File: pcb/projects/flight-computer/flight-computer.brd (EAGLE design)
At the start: 101.6 x 60.6 mm, 92 parts, among them CN1 4U#20329, IC1 ADG609RU, IC2 ATSAMD21E, IC3 ADG609RU, P1 53048-0810, P2 53048-0810, U1 MCP73831/OT, U10 SN74LVC1G08DCKR, U12 MAX31856MUD+, U13 MAX31856MUD+, U2 LP2985IM5-1.8/NOPB, U3 COM-13909, U4 ADXL377, U5 ICM-20948, U6 PCA9306DCUR, U7 SN74LVC1T45DRLR, U8 SN74LVC1T45DRLR, U9 DMP3099L

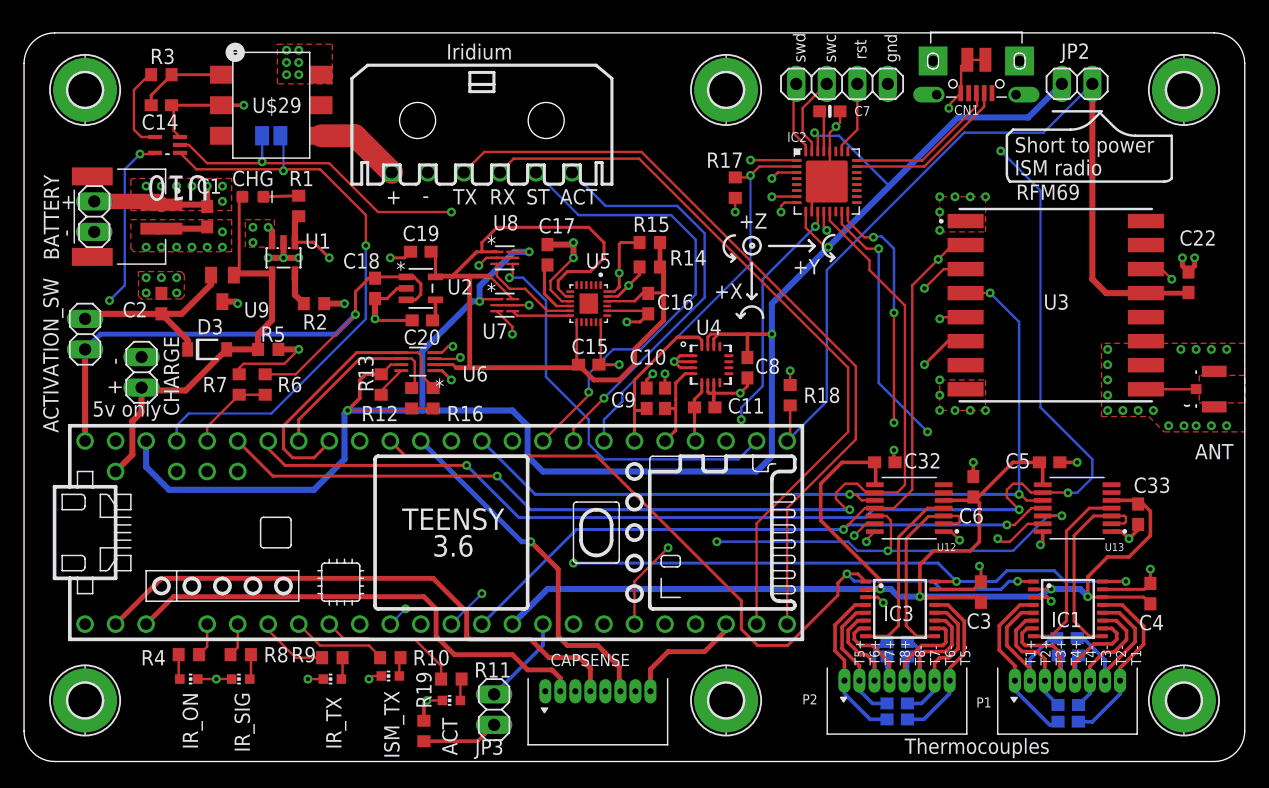
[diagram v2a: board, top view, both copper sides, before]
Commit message: add v1.1 pcb and documentation - added DSP310 barometric pressure sensor - add buzzer - add capacitive sense header - add more interface pins to the safety processor - add arduino pinouts for safety processor and refs on board silk - update flight computer hardware manual - add gerbers for v1.1 boards
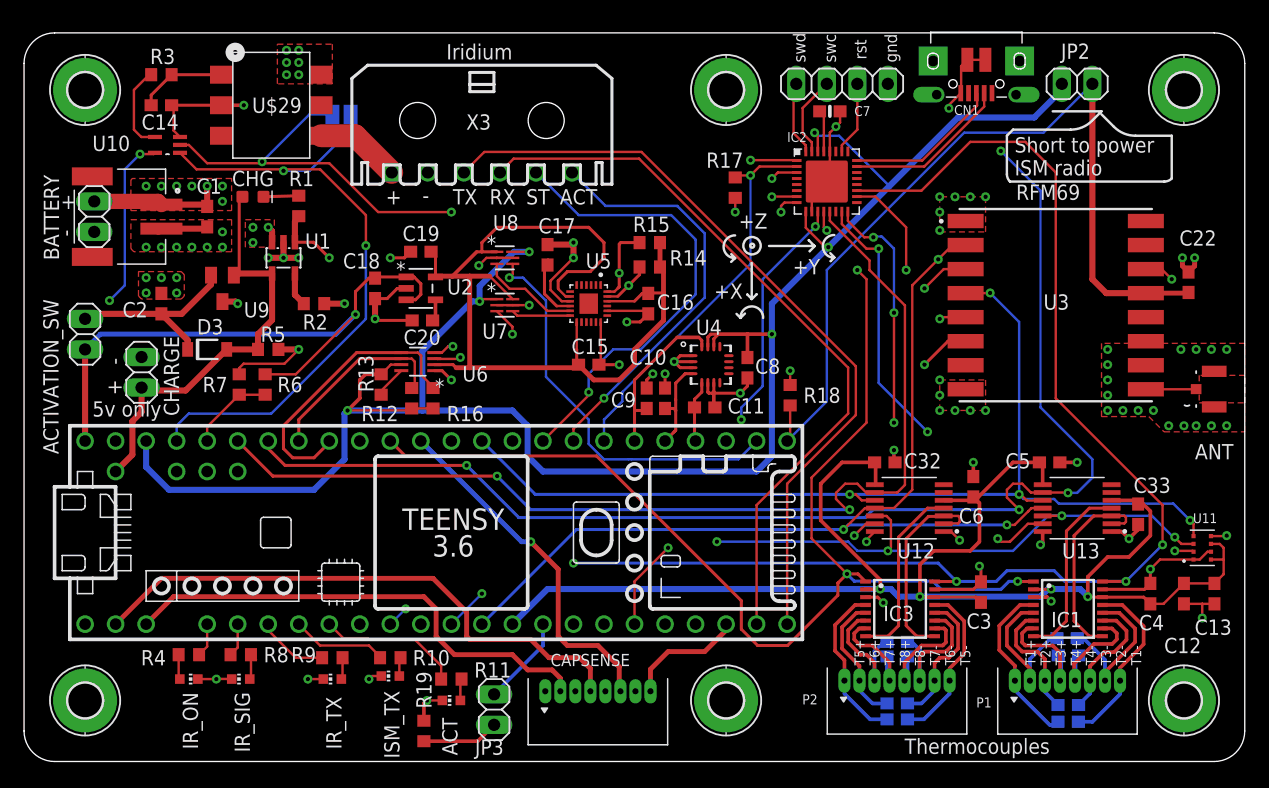
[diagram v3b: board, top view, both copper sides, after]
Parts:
- added C12, C13: 0.1uF, rcl:C0603
- added U11: DPS310XTSA1, DPS310XTSA1:XDCR_DPS310XTSA1
- moved SJ1 6.11 mm to (26.4, 53.8)
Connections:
- net SEC_CS renamed SEC_CTRL_2
- net SEC_EN renamed SEC_CTRL_1
- new net CS_DSP: U$1.8, U11.2
- net 3V3: now also C12.1, C13.1, U11.6, U11.8
- net GND: now also C12.2, C13.2, U11.1, U11.7
- net MISO: now also U11.5
- net MOSI: now also U11.3
- net MUX0: now also IC2.18
- net MUX1: now also IC2.19
- net SCLK: now also U11.4
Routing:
- net CS_DSP: track 0.00 -> 74.5 mm, vias 0 -> 1
- net MUX1: track 73.1 -> 131.4 mm, vias 3 -> 4
- net MUX0: track 67.6 -> 109.1 mm, vias 2 -> 4
- net MISO: track 92.5 -> 112.5 mm, vias 4 -> 5
- net SCLK: track 93.2 -> 109.7 mm, vias 4 -> 5
- net MOSI: track 112.1 -> 124.0 mm, vias 6 -> 7
- net 3V3: track 312.8 -> 324.7 mm
- net GND: track 133.2 -> 142.6 mm, vias 81 -> 82
- net SEC_ACT: track 57.8 -> 63.1 mm
- net PRI_ACT: track 50.1 -> 55.4 mm
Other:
- board text added: "0 CAPSENSE0 1 CAPSENSE1 3 LED1 (IR_ON) 4 LED2 (IR_SIG) 5 LED3 (IR_TX) 6 LED4 (ISM_TX) 7 LED5 (ACT) 8 CS_DSP 9 CS_ISM"
- board text added: "1 CS@TC1 13 CS@TC2 7 SEC_ACT 8 SEC_CTRL_1 0 SEC_CTRL_2 PA14 TC1_FAULT PA15 TC2_FAULT PA17 MUX0 PA18 MUX1"
- board text added: "20 CS@TC1 21 CS@TC2 A8 BAT_SENSE 23 ACT (IRIDIUM ON/OFF) 27 SEC_CTRL_2 28 RESET_ISM 29 INT_ISM 30 CAPSENSE3 31 RIRI (IRIDIUM OUTPUT) 32 TIRI (IRIDIUM INPUT) 33 RADIO_OFF_SIG 39 SEC_CTRL_1"
- board text added: "For SAMD21"
- board text added: "For Teensy"
- board text added: "KREPE Flight Computer V1.1 University of Kentucky 2020 Dr. Alexandre Martin, Dr. Bill Smith, Tyler Nichols, Matt Ruffner, Josh Laredo, Kirsten Ford, Andrew Perry, John Schmidt"
- board text added: "Pin"
- board text added: "X3"
- board text removed: "0 CAPSENSE0 1 CAPSENSE1 3 LED1 (IR_ON) 4 LED2 (IR_SIG) 5 LED3 (IR_TX) 6 LED4 (ISM_TX) 7 LED5 (ACT) 9 CS_ISM"
- board text removed: "20 CS@TC1 21 CS@TC2 A8 BAT_SENSE 23 ACT (IRIDIUM ON/OFF) 28 RESET_ISM 28 INT_ISM 30 CAPSENSE3 31 RIRI (IRIDIUM OUTPUT) 32 TIRI (IRIDIUM INPUT) 33 RADIO_OFF_SIG"
- board text removed: "KREPE Flight Computer V1.1 University of Kentucky 2020 Dr. Alexandre Martin, Dr. Bill Smith, Tyler Nichols, Matt Ruffner, Josh Laredo, Kirsten Ford, Andrew Perry"
